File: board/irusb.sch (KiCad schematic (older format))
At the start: 18 parts, among them IC1 ATTINY45-P, J1 USB_1, Q1 NPN, X1 QUARTZCMS4

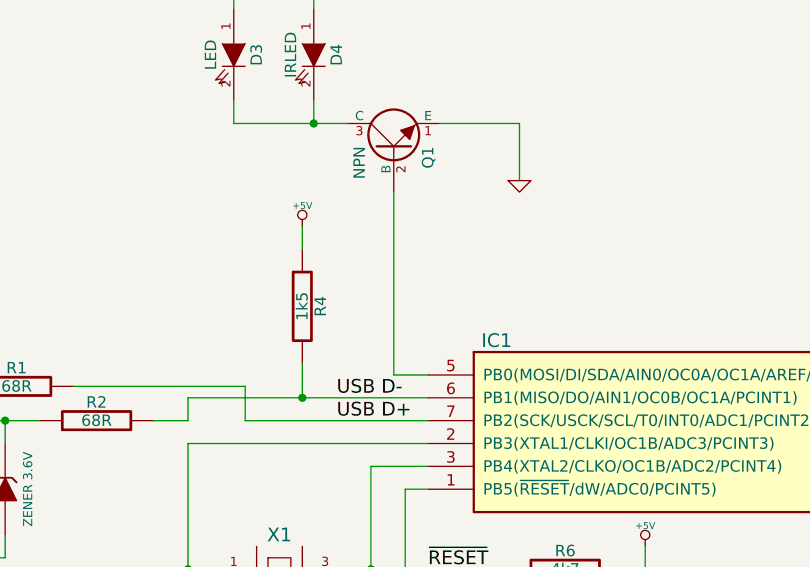
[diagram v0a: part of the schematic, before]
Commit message: added missing base resistor for transistor in schematic
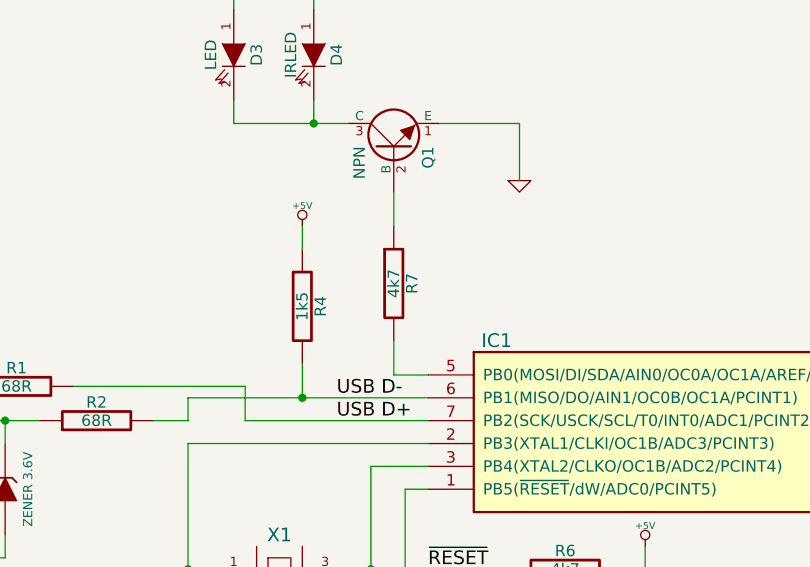
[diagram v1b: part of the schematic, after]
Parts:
- added R7: 4k7, symbol R
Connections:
- net at IC1.5 (PB0(MOSI/DI/SDA/AIN0/OC0A/OC1A/AREF/PCINT0)): now also R7.2; no longer Q1.2 (B)
- new net: Q1.2 (B), R7.1
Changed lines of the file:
@@
-EESchema Schematic File Version 2  date Fri 15 Feb 2013 11:07:17 PM CET
+EESchema Schematic File Version 2  date Sun 24 Feb 2013 10:10:23 PM CET
 LIBS:power
 LIBS:device
@@
 Sheet 1 1
 Title "IRUSB"
-Date "15 feb 2013"
+Date "24 feb 2013"
 Rev ".1"
 Comp ""
@@
 $EndDescr
 Wire Wire Line
+	4050 3700 4050 3550
+Wire Wire Line
 	6900 4850 7550 4850
 Wire Wire Line
 	7550 4850 7550 4800
 Wire Wire Line
-	4050 3550 4050 4350
-Wire Wire Line
-	4050 4350 4200 4350
+	4200 4350 4050 4350
 Wire Wire Line
 	2000 5050 2000 5200
@@
 Wire Wire Line
 	7550 4350 6900 4350
+Wire Wire Line
+	4050 4350 4050 4200
+$Comp
+L R R7
+U 1 1 512A8186
+P 4050 3950
+F 0 "R7" V 4130 3950 50  0000 C CNN
+F 1 "4k7" V 4050 3950 50  0000 C CNN
+	1    4050 3950
+	1    0    0    -1
+$EndComp
 $Comp
 L C C4
